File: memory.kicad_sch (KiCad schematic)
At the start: 4 parts

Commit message: Final PCB Layout
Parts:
- added C15, C16, C17, C18: 1uF, Capacitor_SMD:C_0805_2012Metric_Pad1.18x1.45mm_HandSolder, symbol Device:C_Small
- U6: renamed from U?; footprint Package_DIP:DIP-28_W15.24mm -> Package_DIP:DIP-28_W15.24mm_Socket_LongPads; symbol Memory_RAM:KM62256CLP -> MCD_Symbols:AS6C62256; Name RAM1 -> RAM_LOW
- U7: renamed from U?; footprint Package_DIP:DIP-28_W15.24mm -> Package_DIP:DIP-28_W15.24mm_Socket_LongPads; symbol Memory_RAM:KM62256CLP -> MCD_Symbols:AS6C62256; Name RAM2 -> RAM_HIGH
- U8: renamed from U?; footprint Package_LCC:PLCC-32_11.4x14.0mm_P1.27mm -> Package_LCC:PLCC-32_THT-Socket; symbol Memory_EEPROM:28C256 -> MCD_Symbols:AT28C256; Name ROM1 -> ROM_LOW
- U9: renamed from U?; footprint Package_LCC:PLCC-32_11.4x14.0mm_P1.27mm -> Package_LCC:PLCC-32_THT-Socket; symbol Memory_EEPROM:28C256 -> MCD_Symbols:AT28C256; Name ROM2 -> ROM_HIGH
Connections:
- net +5V: now also U8.32 (VCC), U9.32 (VCC), C15.2, C16.2, C17.2, C18.2; no longer U8.28 (VCC), U9.28 (VCC)
- net A1: now also U6.10 (A0), U7.10 (A0), U8.11 (A0), U9.11 (A0); no longer U6.9 (A1), U7.9 (A1), U8.9 (A1), U9.9 (A1)
- net A10: now also U6.24 (A9), U7.24 (A9), U8.28 (A9), U9.28 (A9); no longer U6.21 (A10), U7.21 (A10), U8.21 (A10), U9.21 (A10)
- net A11: now also U6.21 (A10), U7.21 (A10), U8.24 (A10), U9.24 (A10); no longer U6.23 (A11), U7.23 (A11), U8.23 (A11), U9.23 (A11)
- net A12: now also U6.23 (A11), U7.23 (A11), U8.27 (A11), U9.27 (A11); no longer U6.2 (A12), U7.2 (A12), U8.2 (A12), U9.2 (A12)
- net A13: now also U6.2 (A12), U7.2 (A12), U8.3 (A12), U9.3 (A12); no longer U6.26 (A13), U7.26 (A13), U8.26 (A13), U9.26 (A13)
- net A14: now also U6.26 (A13), U7.26 (A13), U8.30 (A13), U9.30 (A13); no longer U6.1 (A14), U7.1 (A14), U8.1 (A14), U9.1 (A14)
- net A2: now also U6.9 (A1), U7.9 (A1), U8.10 (A1), U9.10 (A1); no longer U6.8 (A2), U7.8 (A2), U8.8 (A2), U9.8 (A2)
- net A3: now also U6.8 (A2), U7.8 (A2), U8.9 (A2), U9.9 (A2); no longer U6.7 (A3), U7.7 (A3), U8.7 (A3), U9.7 (A3)
- net A4: now also U6.7 (A3), U7.7 (A3), U8.8 (A3), U9.8 (A3); no longer U6.6 (A4), U7.6 (A4), U8.6 (A4), U9.6 (A4)
- net A5: now also U6.6 (A4), U7.6 (A4), U8.7 (A4), U9.7 (A4); no longer U6.5 (A5), U7.5 (A5), U8.5 (A5), U9.5 (A5)
- net A6: now also U6.5 (A5), U7.5 (A5), U8.6 (A5), U9.6 (A5); no longer U6.4 (A6), U7.4 (A6), U8.4 (A6), U9.4 (A6)
- net A7: now also U6.4 (A6), U7.4 (A6), U8.5 (A6), U9.5 (A6); no longer U6.3 (A7), U7.3 (A7), U8.3 (A7), U9.3 (A7)
- net A8: now also U6.3 (A7), U7.3 (A7), U8.4 (A7), U9.4 (A7); no longer U6.25 (A8), U7.25 (A8), U8.25 (A8), U9.25 (A8)
- net A9: now also U6.25 (A8), U7.25 (A8), U8.29 (A8), U9.29 (A8); no longer U6.24 (A9), U7.24 (A9), U8.24 (A9), U9.24 (A9)
- net D0: now also U8.13 (D0); no longer U7.11 (Q0), U8.11 (D0), U9.11 (D0)
- net D1: now also U8.14 (D1); no longer U7.12 (Q1), U8.12 (D1), U9.12 (D1)
- net D2: now also U8.15 (D2); no longer U7.13 (Q2), U8.13 (D2), U9.13 (D2)
- net D3: now also U8.18 (D3); no longer U7.15 (Q3), U8.15 (D3), U9.15 (D3)
- net D4: now also U8.19 (D4); no longer U7.16 (Q4), U8.16 (D4), U9.16 (D4)
- net D5: now also U8.20 (D5); no longer U7.17 (Q5), U8.17 (D5), U9.17 (D5)
- net D6: now also U8.21 (D6); no longer U7.18 (Q6), U8.18 (D6), U9.18 (D6)
- net D7: now also U8.22 (D7); no longer U7.19 (Q7), U8.19 (D7), U9.19 (D7)
- net GND: now also U8.16 (GND), U9.16 (GND), C15.1, C16.1, C17.1, C18.1; no longer U8.14 (GND), U9.14 (GND)
- net ROM1_~{CS}: now also U8.23 (~{CE}); no longer U8.20 (~{CS})
- net ROM1_~{OE}: now also U8.25 (~{OE}); no longer U8.22 (~{OE})
- net ROM1_~{WE}: now also U8.31 (~{WE}); no longer U8.27 (~{WE})
- net ROM2_~{CS}: now also U9.23 (~{CE}); no longer U9.20 (~{CS})
- net ROM2_~{OE}: now also U9.25 (~{OE}); no longer U9.22 (~{OE})
- net ROM2_~{WE}: now also U9.31 (~{WE}); no longer U9.27 (~{WE})
- removed net A0: U6.10 (A0), U7.10 (A0), U8.10 (A0), U9.10 (A0)
- new net A15: U6.1 (A14), U7.1 (A14), U8.2 (A14), U9.2 (A14)
- new net D10: U7.13 (DQ2), U9.15 (D2)
- new net D11: U7.15 (DQ3), U9.18 (D3)
- new net D12: U7.16 (DQ4), U9.19 (D4)
- new net D13: U7.17 (DQ5), U9.20 (D5)
- new net D14: U7.18 (DQ6), U9.21 (D6)
- new net D15: U7.19 (DQ7), U9.22 (D7)
- new net D8: U7.11 (DQ0), U9.13 (D0)
- new net D9: U7.12 (DQ1), U9.14 (D1)
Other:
- company: (none) -> Jackson Miller
- title: (none) -> Memory Connections
- moved on the sheet: U6, U7

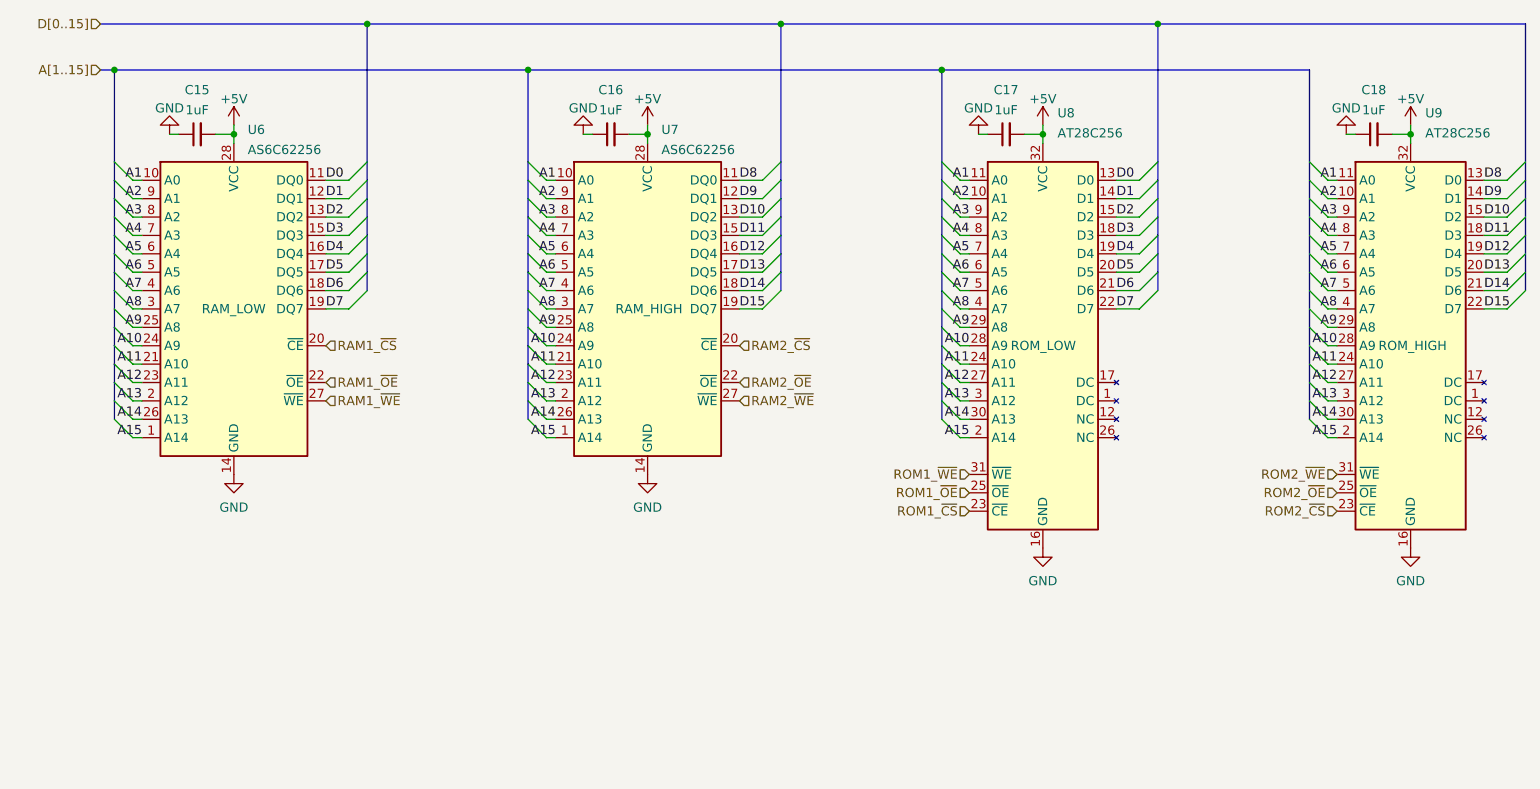
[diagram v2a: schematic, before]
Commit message: Rename Memory to match High/Low
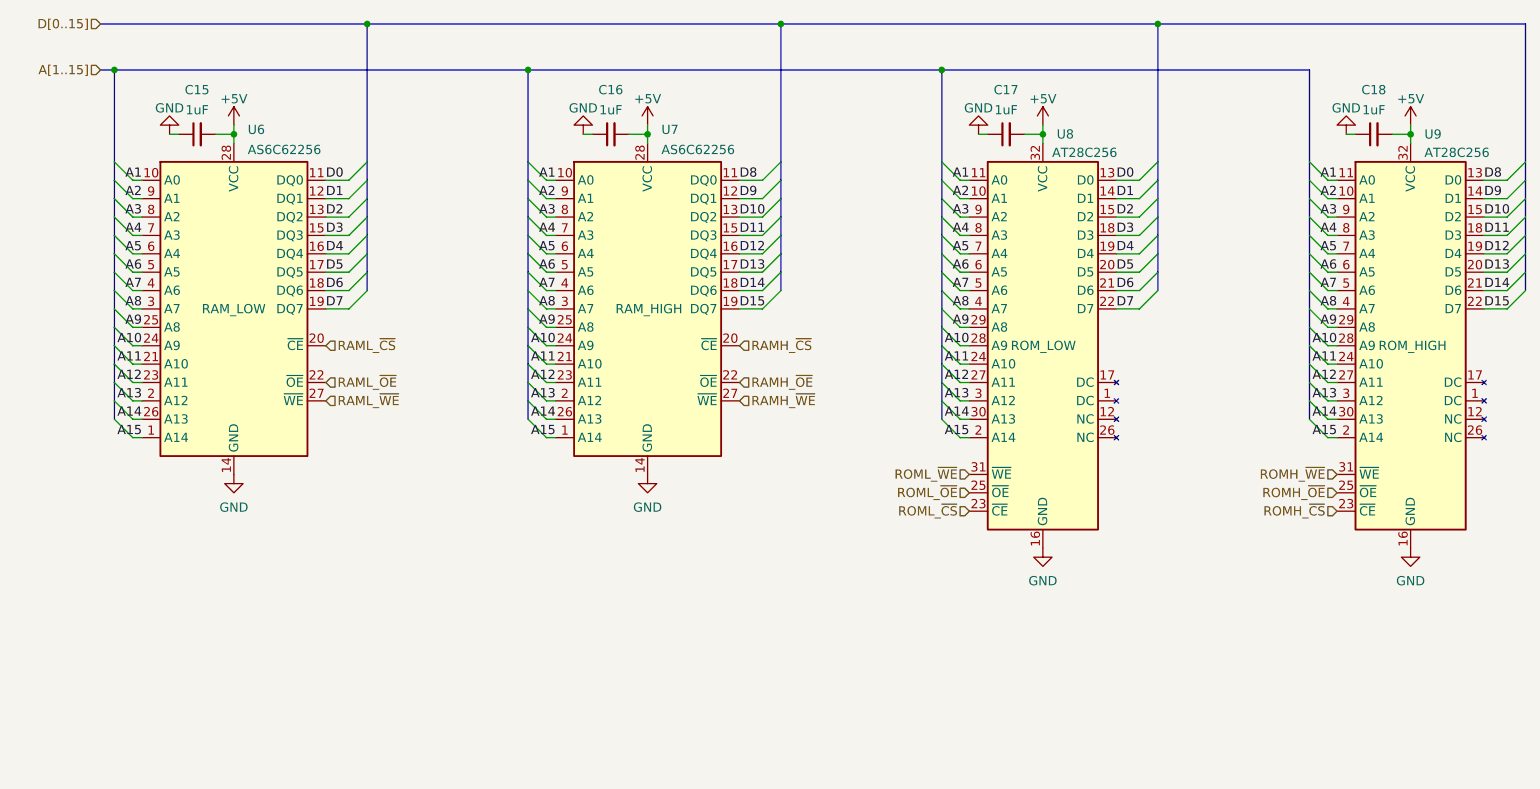
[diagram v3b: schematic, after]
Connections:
- net RAM1_~{CS} renamed RAML_~{CS}
- net RAM1_~{OE} renamed RAML_~{OE}
- net RAM1_~{WE} renamed RAML_~{WE}
- net RAM2_~{CS} renamed RAMH_~{CS}
- net RAM2_~{OE} renamed RAMH_~{OE}
- net RAM2_~{WE} renamed RAMH_~{WE}
- net ROM1_~{CS} renamed ROML_~{CS}
- net ROM1_~{OE} renamed ROML_~{OE}
- net ROM1_~{WE} renamed ROML_~{WE}
- net ROM2_~{CS} renamed ROMH_~{CS}
- net ROM2_~{OE} renamed ROMH_~{OE}
- net ROM2_~{WE} renamed ROMH_~{WE}
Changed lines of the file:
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@@
     (effects (font (size 1.27 1.27)) (justify right bottom))
   )
-  (hierarchical_label "ROM1_~{WE}" (shape input) (at 145.415 81.28 180)
+  (hierarchical_label "ROML_~{WE}" (shape input) (at 145.415 81.28 180)
     (effects (font (size 1.27 1.27)) (justify right))
   )
-  (hierarchical_label "ROM2_~{OE}" (shape input) (at 196.215 83.82 180)
+  (hierarchical_label "ROMH_~{OE}" (shape input) (at 196.215 83.82 180)
     (effects (font (size 1.27 1.27)) (justify right))
   )
-  (hierarchical_label "RAM1_~{OE}" (shape input) (at 56.515 68.58 0)
+  (hierarchical_label "RAML_~{OE}" (shape input) (at 56.515 68.58 0)
     (effects (font (size 1.27 1.27)) (justify left))
   )
-  (hierarchical_label "ROM1_~{CS}" (shape input) (at 145.415 86.36 180)
+  (hierarchical_label "ROML_~{CS}" (shape input) (at 145.415 86.36 180)
     (effects (font (size 1.27 1.27)) (justify right))
   )
-  (hierarchical_label "ROM1_~{OE}" (shape input) (at 145.415 83.82 180)
+  (hierarchical_label "ROML_~{OE}" (shape input) (at 145.415 83.82 180)
     (effects (font (size 1.27 1.27)) (justify right))
   )
-  (hierarchical_label "RAM2_~{CS}" (shape input) (at 113.665 63.5 0)
+  (hierarchical_label "RAMH_~{CS}" (shape input) (at 113.665 63.5 0)
     (effects (font (size 1.27 1.27)) (justify left))
   )
-  (hierarchical_label "RAM1_~{CS}" (shape input) (at 56.515 63.5 0)
+  (hierarchical_label "RAML_~{CS}" (shape input) (at 56.515 63.5 0)
     (effects (font (size 1.27 1.27)) (justify left))
   )
@@
     (effects (font (size 1.27 1.27)) (justify right))
   )
-  (hierarchical_label "RAM2_~{WE}" (shape input) (at 113.665 71.12 0)
+  (hierarchical_label "RAMH_~{WE}" (shape input) (at 113.665 71.12 0)
     (effects (font (size 1.27 1.27)) (justify left))
   )
-  (hierarchical_label "ROM2_~{CS}" (shape input) (at 196.215 86.36 180)
+  (hierarchical_label "ROMH_~{CS}" (shape input) (at 196.215 86.36 180)
     (effects (font (size 1.27 1.27)) (justify right))
   )
-  (hierarchical_label "RAM1_~{WE}" (shape input) (at 56.515 71.12 0)
+  (hierarchical_label "RAML_~{WE}" (shape input) (at 56.515 71.12 0)
     (effects (font (size 1.27 1.27)) (justify left))
   )
-  (hierarchical_label "ROM2_~{WE}" (shape input) (at 196.215 81.28 180)
+  (hierarchical_label "ROMH_~{WE}" (shape input) (at 196.215 81.28 180)
     (effects (font (size 1.27 1.27)) (justify right))
   )
-  (hierarchical_label "RAM2_~{OE}" (shape input) (at 113.665 68.58 0)
+  (hierarchical_label "RAMH_~{OE}" (shape input) (at 113.665 68.58 0)
     (effects (font (size 1.27 1.27)) (justify left))
   )
   (symbol (lib_id "MCD_Symbols:AT28C256") (at 206.375 63.5 0) (unit 1)
     (in_bom yes) (on_board yes)
-    (property "Reference" "U9" (id 0) (at 208.3944 31.3583 0)
+    (property "Reference" "U9" (id 0) (at 208.28 34.29 0)
       (effects (font (size 1.27 1.27)) (justify left))
     )
-    (property "Value" "AT28C256" (id 1) (at 208.3944 34.1334 0)
+    (property "Value" "AT28C256" (id 1) (at 208.28 36.83 0)
       (effects (font (size 1.27 1.27)) (justify left))
     )
@@
   (symbol (lib_id "MCD_Symbols:AT28C256") (at 155.575 63.5 0) (unit 1)
     (in_bom yes) (on_board yes)
-    (property "Reference" "U8" (id 0) (at 157.5944 31.3583 0)
+    (property "Reference" "U8" (id 0) (at 157.48 34.29 0)
       (effects (font (size 1.27 1.27)) (justify left))
     )
-    (property "Value" "AT28C256" (id 1) (at 157.5944 34.1334 0)
+    (property "Value" "AT28C256" (id 1) (at 156.845 36.83 0)
       (effects (font (size 1.27 1.27)) (justify left))
     )
